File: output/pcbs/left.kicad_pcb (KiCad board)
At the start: 2 copper layers, 137.1 x 116.2 mm, 79 parts

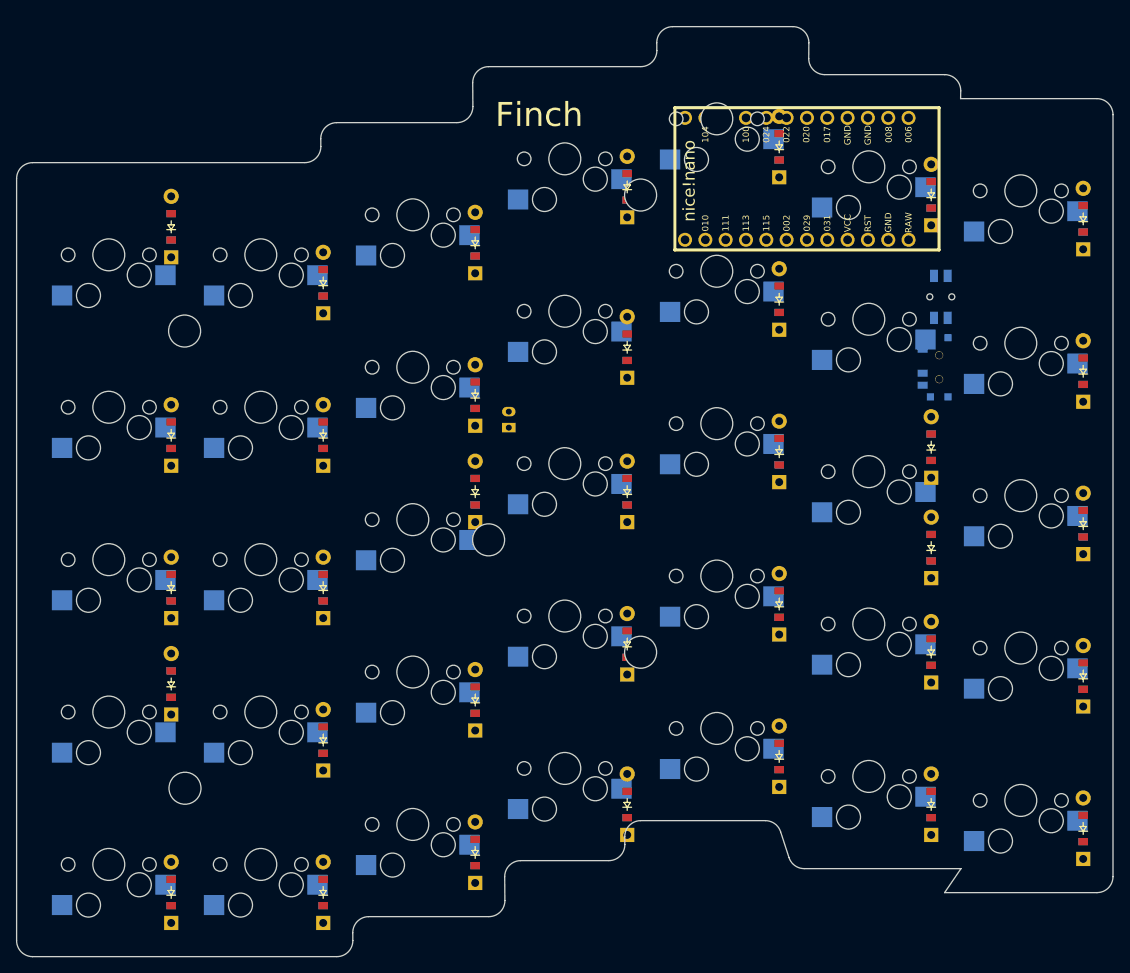
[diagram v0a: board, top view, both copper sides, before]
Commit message: updated diode pos., controller, and outlines
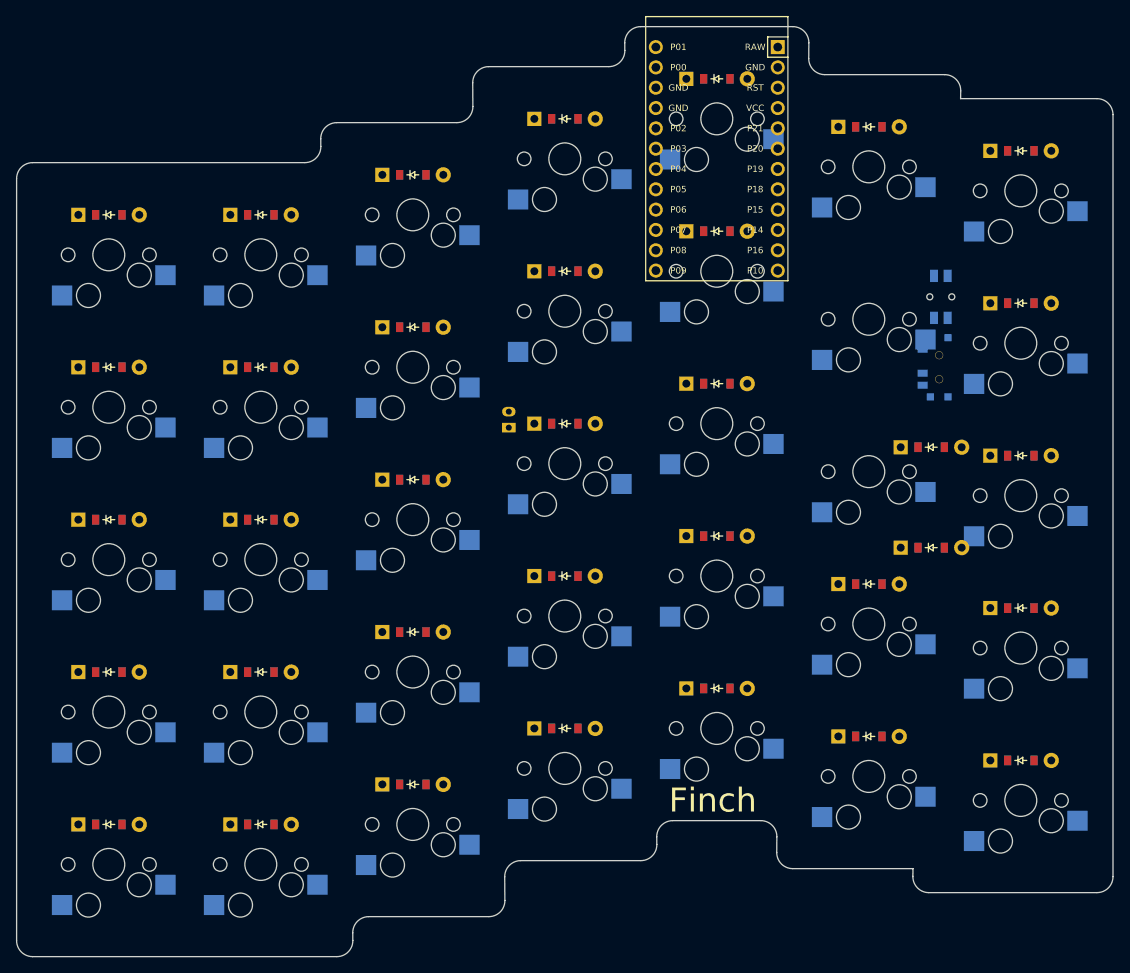
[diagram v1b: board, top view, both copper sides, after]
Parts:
- removed ? (x5): , HOLE_M2_TH
- MCU1: value nice_nano -> (none); footprint nice_nano -> ProMicro
- moved D31 110.0 mm to (214.0, 98.9), turned to 0 degrees
- moved D32 106.6 mm to (214.0, 79.9), turned to 0 degrees
- moved D24 87.6 mm to (176.0, 70.9), turned to 0 degrees
- moved D25 87.6 mm to (176.0, 51.8), turned to 0 degrees
- moved D33 80.4 mm to (214.0, 60.8), turned to 0 degrees
- moved D4 70.9 mm to (100.0, 87.8), turned to 0 degrees
- moved D5 70.9 mm to (100.0, 68.8), turned to 0 degrees
- moved D9 66.3 mm to (119.0, 87.8), turned to 0 degrees
- moved D10 66.3 mm to (119.0, 68.8), turned to 0 degrees
- moved D34 58.6 mm to (202.8, 97.9), turned to 0 degrees
- moved D11 49.3 mm to (138.0, 140.0), turned to 0 degrees
- moved D12 49.3 mm to (138.0, 121.0), turned to 0 degrees
- moved D35 45.5 mm to (202.8, 110.4), turned to 0 degrees
- moved D29 40.7 mm to (214.0, 137.0), turned to 0 degrees
- moved D26 37.8 mm to (195.0, 134.0), turned to 0 degrees
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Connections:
- net P009 renamed P1
- net P010 renamed P0
- net P011 renamed P14
- net P104 renamed P16
- net P106 renamed P10
- D10 pad 1: P20 -> P15
- D10 pad 2: third_bottom -> second_num
- D11 pad 1: P18 -> P21
- D11 pad 2: third_top -> third_mod
- D12 pad 1: P15 -> P20
- D12 pad 2: third_num -> third_bottom
- D13 pad 1: P20 -> P19
- D13 pad 2: fourth_bottom -> third_home
- D14 pad 1: P19 -> P18
- D14 pad 2: fourth_home -> third_top
- D15 pad 2: fourth_num -> third_num
- D16 pad 2: fifth_mod -> fourth_mod
- D17 pad 2: fifth_bottom -> fourth_bottom
- D18 pad 2: fifth_home -> fourth_home
- D19 pad 2: fifth_top -> fourth_top
- D2 pad 1: P19 -> P20
- D2 pad 2: first_home -> first_bottom
- D20 pad 2: fifth_num -> fourth_num
- D21 pad 2: sixth_mod -> fifth_mod
- D22 pad 2: sixth_bottom -> fifth_bottom
- D23 pad 1: P15 -> P19
- D23 pad 2: sixth_num -> fifth_home
- D24 pad 1: P21 -> P18
- D24 pad 2: seventh_mod -> fifth_top
- D25 pad 1: P20 -> P15
- D25 pad 2: seventh_bottom -> fifth_num
- D26 pad 1: P19 -> P21
- D26 pad 2: seventh_home -> sixth_mod
- D27 pad 1: P18 -> P20
- D27 pad 2: seventh_top -> sixth_bottom
- D28 pad 2: seventh_num -> sixth_num
- D29 pad 1: P18 -> P21
- D29 pad 2: sixth_top -> seventh_mod
- D3 pad 1: P18 -> P19
- D3 pad 2: first_top -> first_home
- D30 pad 1: P19 -> P20
- D30 pad 2: sixth_home -> seventh_bottom
- D31 pad 1: P20 -> P19
- D31 pad 2: first_bottom -> seventh_home
- D32 pad 1: P15 -> P18
- D32 pad 2: first_num -> seventh_top
- D33 pad 1: P19 -> P15
- D33 pad 2: third_home -> seventh_num
- D34 pad 1: P21 -> P18
- D34 pad 2: fourth_mod -> sixth_top
- D35 pad 1: P18 -> P19
- D35 pad 2: fourth_top -> sixth_home
- D4 pad 1: P21 -> P18
- D4 pad 2: second_mod -> first_top
- D5 pad 1: P20 -> P15
- D5 pad 2: second_bottom -> first_num
- D6 pad 1: P19 -> P21
- D6 pad 2: second_home -> second_mod
- D7 pad 1: P18 -> P20
- D7 pad 2: second_top -> second_bottom
- D8 pad 1: P15 -> P19
- D8 pad 2: second_num -> second_home
- D9 pad 1: P21 -> P18
- D9 pad 2: third_mod -> second_top
- MCU1 pad 1: P006 -> RAW
- MCU1 pad 15: P111 -> GND
- MCU1 pad 16: P113 -> GND
- MCU1 pad 17: P115 -> P2
- MCU1 pad 18: P002 -> P3
- MCU1 pad 19: P029 -> P4
- MCU1 pad 2: P008 -> GND
- MCU1 pad 20: P031 -> P5
- MCU1 pad 21: VCC -> P6
- MCU1 pad 22: RST -> P7
- MCU1 pad 23: GND -> P8
- MCU1 pad 24: RAW -> P9
- MCU1 pad 3: GND -> RST
- MCU1 pad 4: GND -> VCC
- MCU1 pad 5: P017 -> P21
- MCU1 pad 6: P020 -> P20
- MCU1 pad 7: P022 -> P19
- MCU1 pad 8: P024 -> P18
- MCU1 pad 9: P100 -> P15
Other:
- outline, holes or cut-outs redrawn

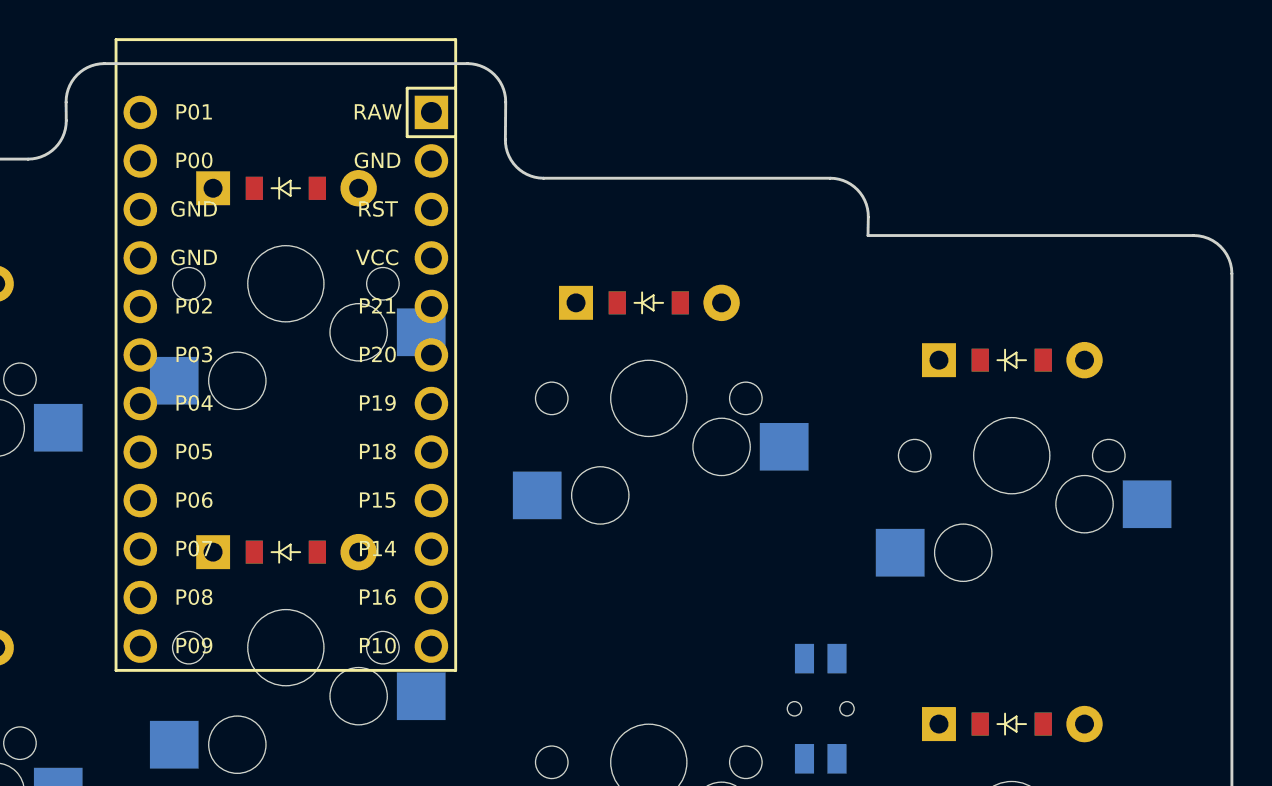
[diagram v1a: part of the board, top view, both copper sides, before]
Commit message: Fixed controller position
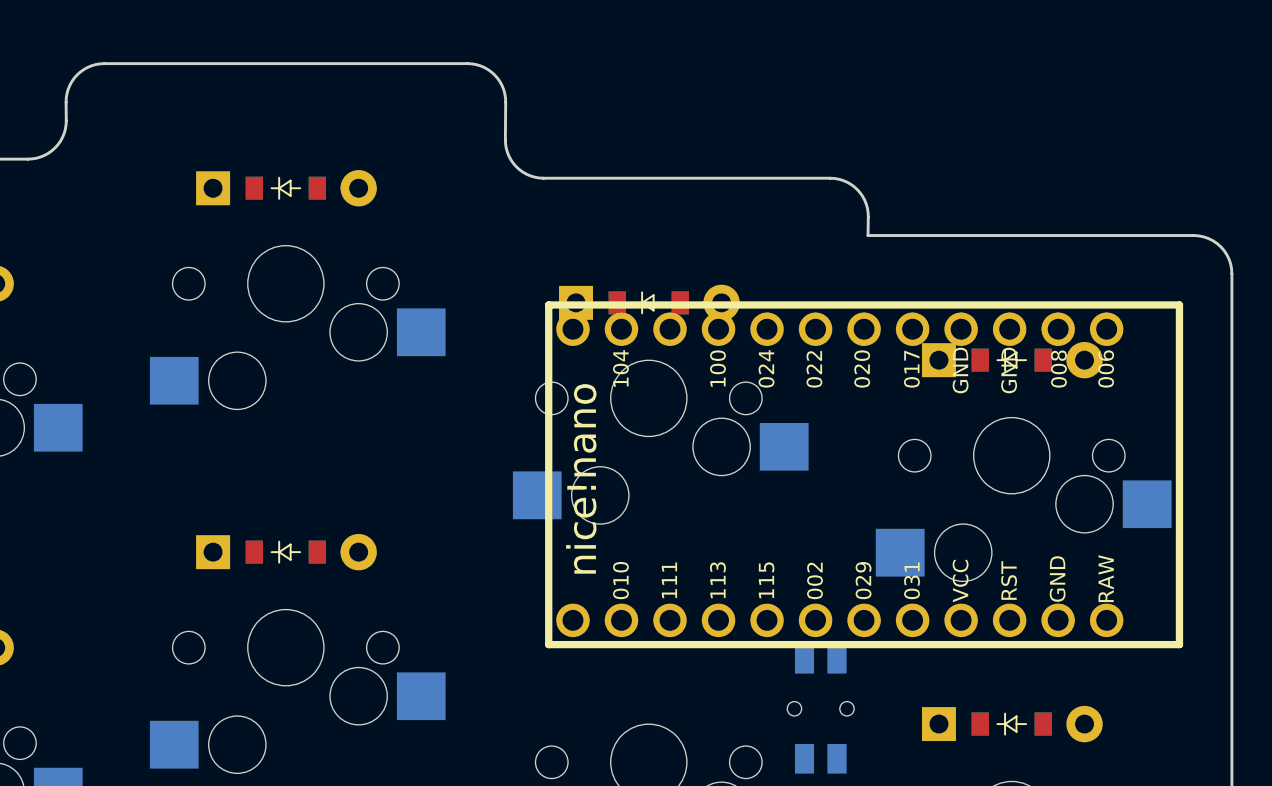
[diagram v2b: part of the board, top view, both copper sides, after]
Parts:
- MCU1: value (none) -> nice_nano; footprint ProMicro -> nice_nano
- moved MCU1 29.4 mm to (205.0, 66.8), turned to -180 degrees
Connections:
- net P0 renamed P010
- net P1 renamed P009
- net P10 renamed P106
- net P14 renamed P011
- net P16 renamed P104
- MCU1 pad 1: RAW -> P006
- MCU1 pad 15: GND -> P111
- MCU1 pad 16: GND -> P113
- MCU1 pad 17: P2 -> P115
- MCU1 pad 18: P3 -> P002
- MCU1 pad 19: P4 -> P029
- MCU1 pad 2: GND -> P008
- MCU1 pad 20: P5 -> P031
- MCU1 pad 21: P6 -> VCC
- MCU1 pad 22: P7 -> RST
- MCU1 pad 23: P8 -> GND
- MCU1 pad 24: P9 -> RAW
- MCU1 pad 3: RST -> GND
- MCU1 pad 4: VCC -> GND
- MCU1 pad 5: P21 -> P017
- MCU1 pad 6: P20 -> P020
- MCU1 pad 7: P19 -> P022
- MCU1 pad 8: P18 -> P024
- MCU1 pad 9: P15 -> P100

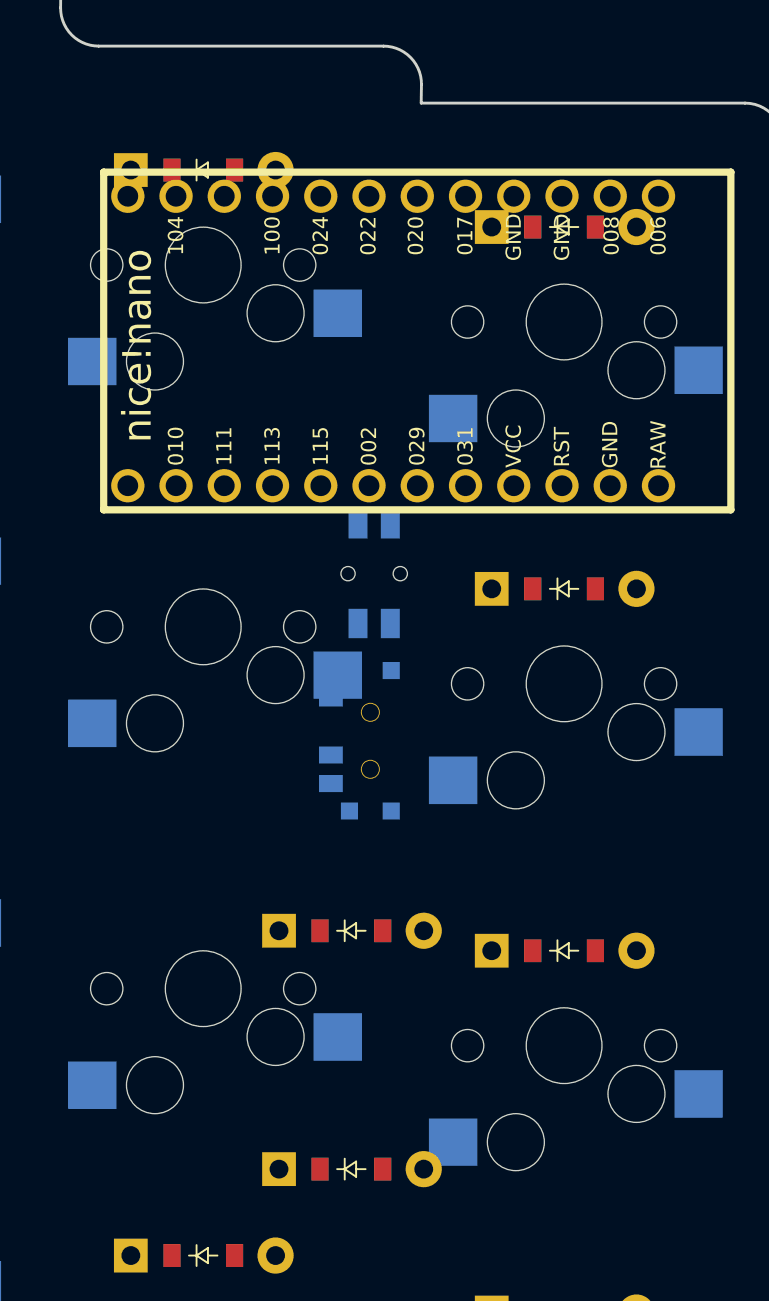
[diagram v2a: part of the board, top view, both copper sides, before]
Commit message: fixed diodes in conflict with controller
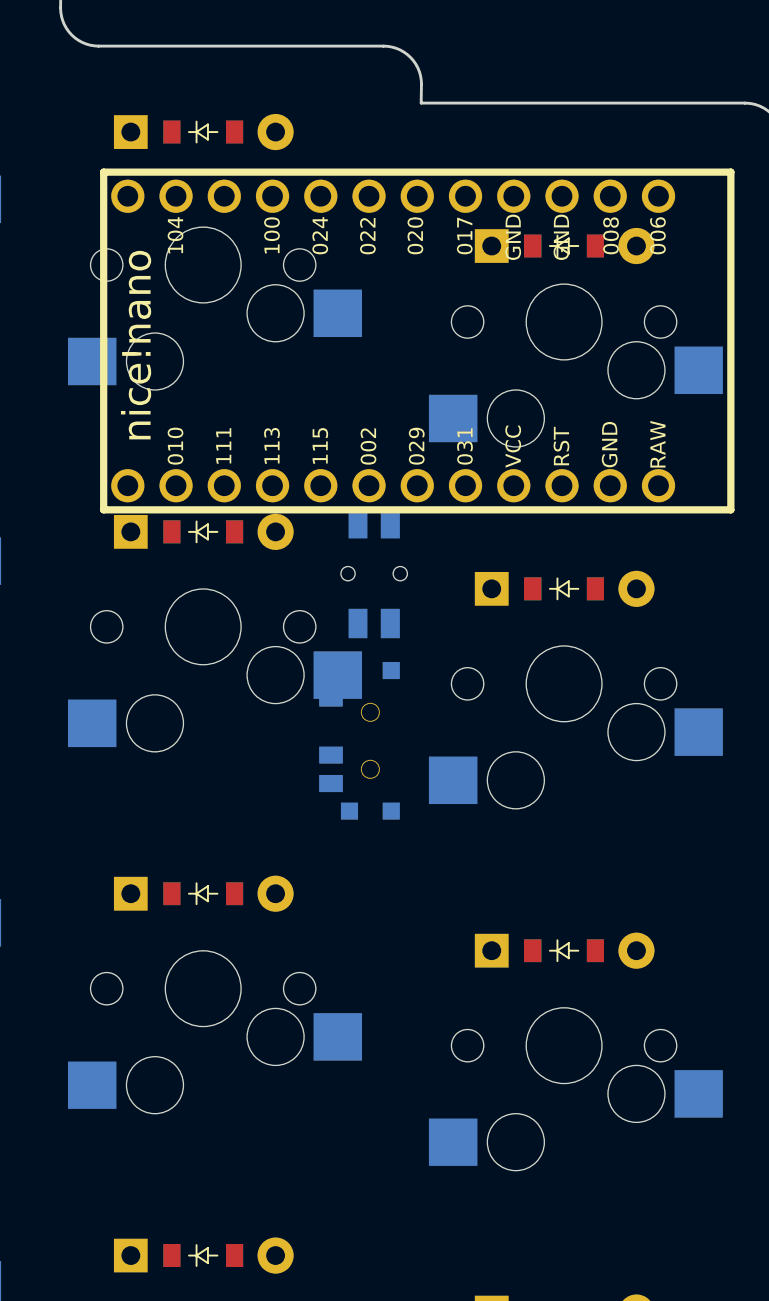
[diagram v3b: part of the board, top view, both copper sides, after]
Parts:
- moved D29 63.1 mm to (195.0, 76.9)
- moved D35 49.9 mm to (214.0, 61.8)
- moved D34 42.8 mm to (195.0, 55.8)
- moved D28 38.1 mm to (195.0, 95.9)
- moved D30 19.0 mm to (214.0, 137.0)
- moved D31 19.0 mm to (214.0, 118.0)
- moved D32 19.0 mm to (214.0, 98.9)
- moved D33 19.0 mm to (214.0, 79.9)
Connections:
- D28 pad 1: P15 -> P19
- D28 pad 2: sixth_num -> sixth_home
- D29 pad 1: P21 -> P18
- D29 pad 2: seventh_mod -> sixth_top
- D30 pad 1: P20 -> P21
- D30 pad 2: seventh_bottom -> seventh_mod
- D31 pad 1: P19 -> P20
- D31 pad 2: seventh_home -> seventh_bottom
- D32 pad 1: P18 -> P19
- D32 pad 2: seventh_top -> seventh_home
- D33 pad 1: P15 -> P18
- D33 pad 2: seventh_num -> seventh_top
- D34 pad 1: P18 -> P15
- D34 pad 2: sixth_top -> sixth_num
- D35 pad 1: P19 -> P15
- D35 pad 2: sixth_home -> seventh_num
